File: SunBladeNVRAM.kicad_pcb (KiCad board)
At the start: 2 copper layers, 36.5 x 18.5 mm, 10 parts, among them J1 Conn_01x14_Pin, J2 Conn_01x14_Pin, J3 Conn_01x02_Pin, J4 Conn_01x02_Pin, J5 Conn_01x01_Pin, J6 Conn_01x01_Pin, J7 Conn_01x01_Pin, J8 Conn_01x01_Pin, U1 M48T59Y-70MH1, Y1 32.768 kHz

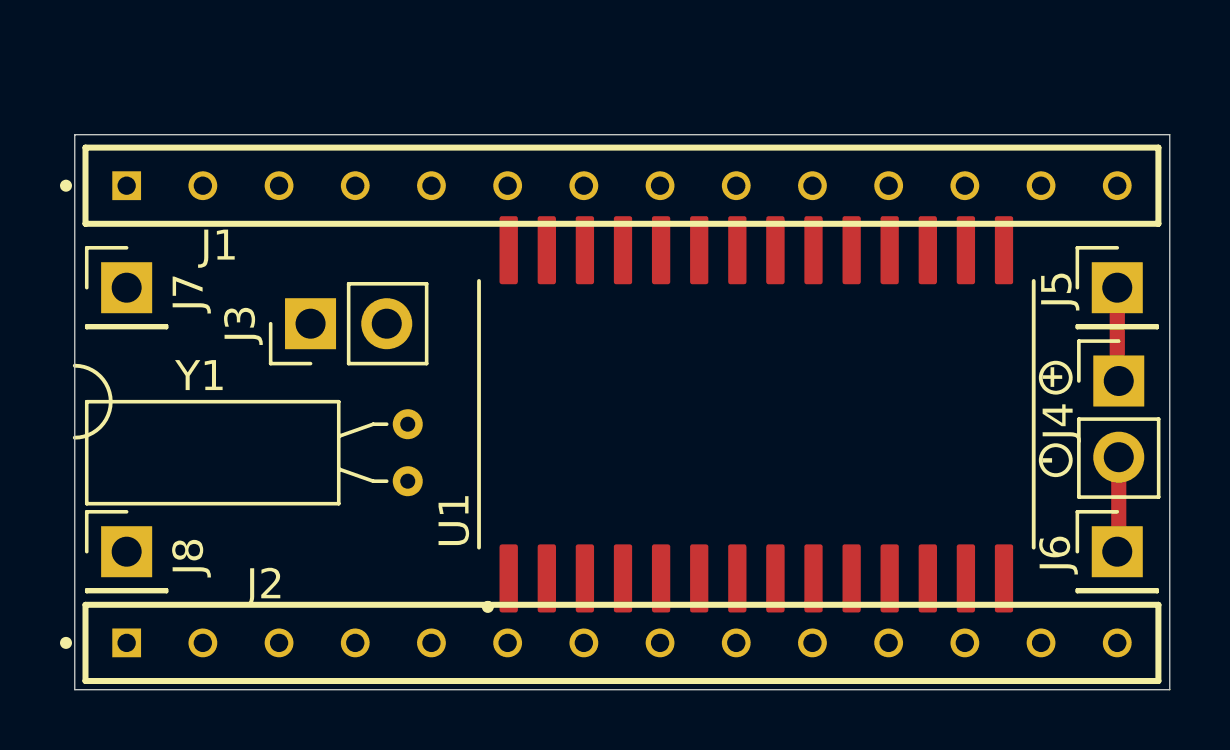
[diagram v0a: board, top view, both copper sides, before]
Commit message: fix pin numbers on SAMTEC 1x14 footprint
Also, remove some of the silkscreen on the SAMTEC
1x14 headers so that it doesn't overlap the M48T59Y
footprint.
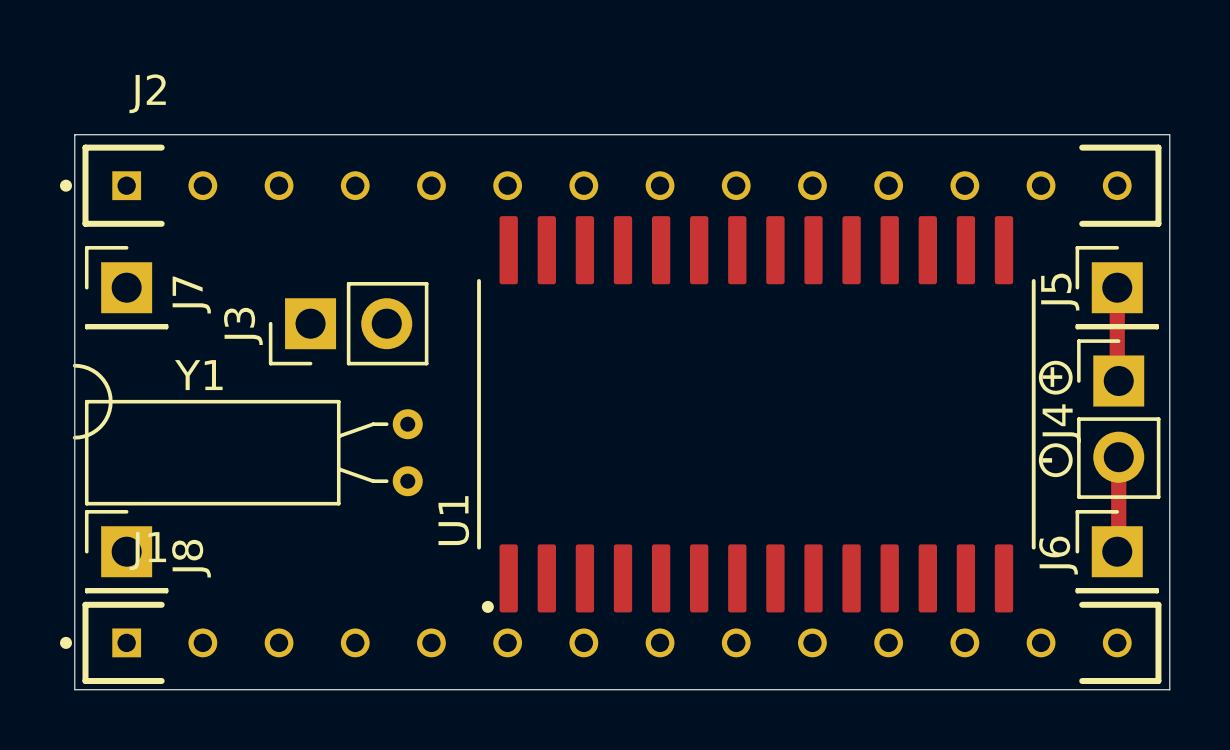
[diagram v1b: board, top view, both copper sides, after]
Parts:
- moved J1 15.2 mm to (85.0, 86.7)
- moved J2 15.2 mm to (85.0, 71.5)
